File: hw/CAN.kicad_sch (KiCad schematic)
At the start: 16 parts, among them IC1 MCP2518FDT-E_SL, IC2 MCP2518FDT-E_SL, IC7 ADM3050EBRIZ, IC8 ADM3050EBRIZ, Y1 ABM8-20.000MHZ-10-B1U-T, Y2 ABM8-20.000MHZ-10-B1U-T

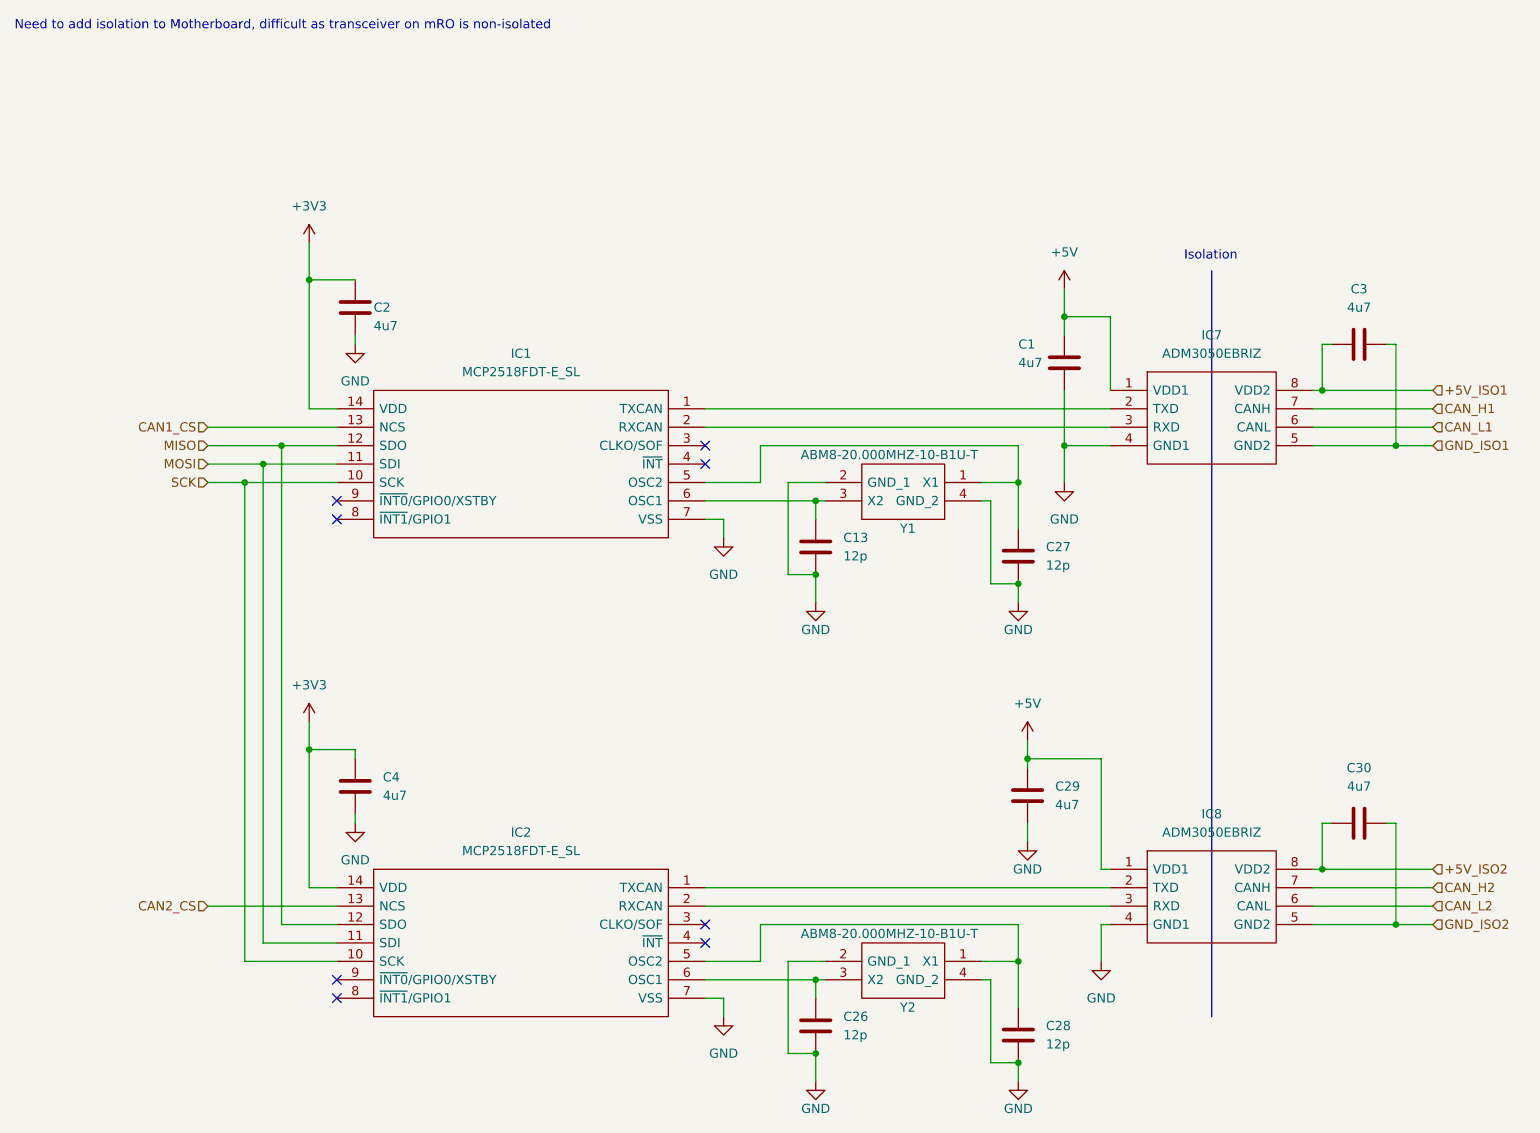
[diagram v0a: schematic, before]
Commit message: connected interrupt pins to CAN controller
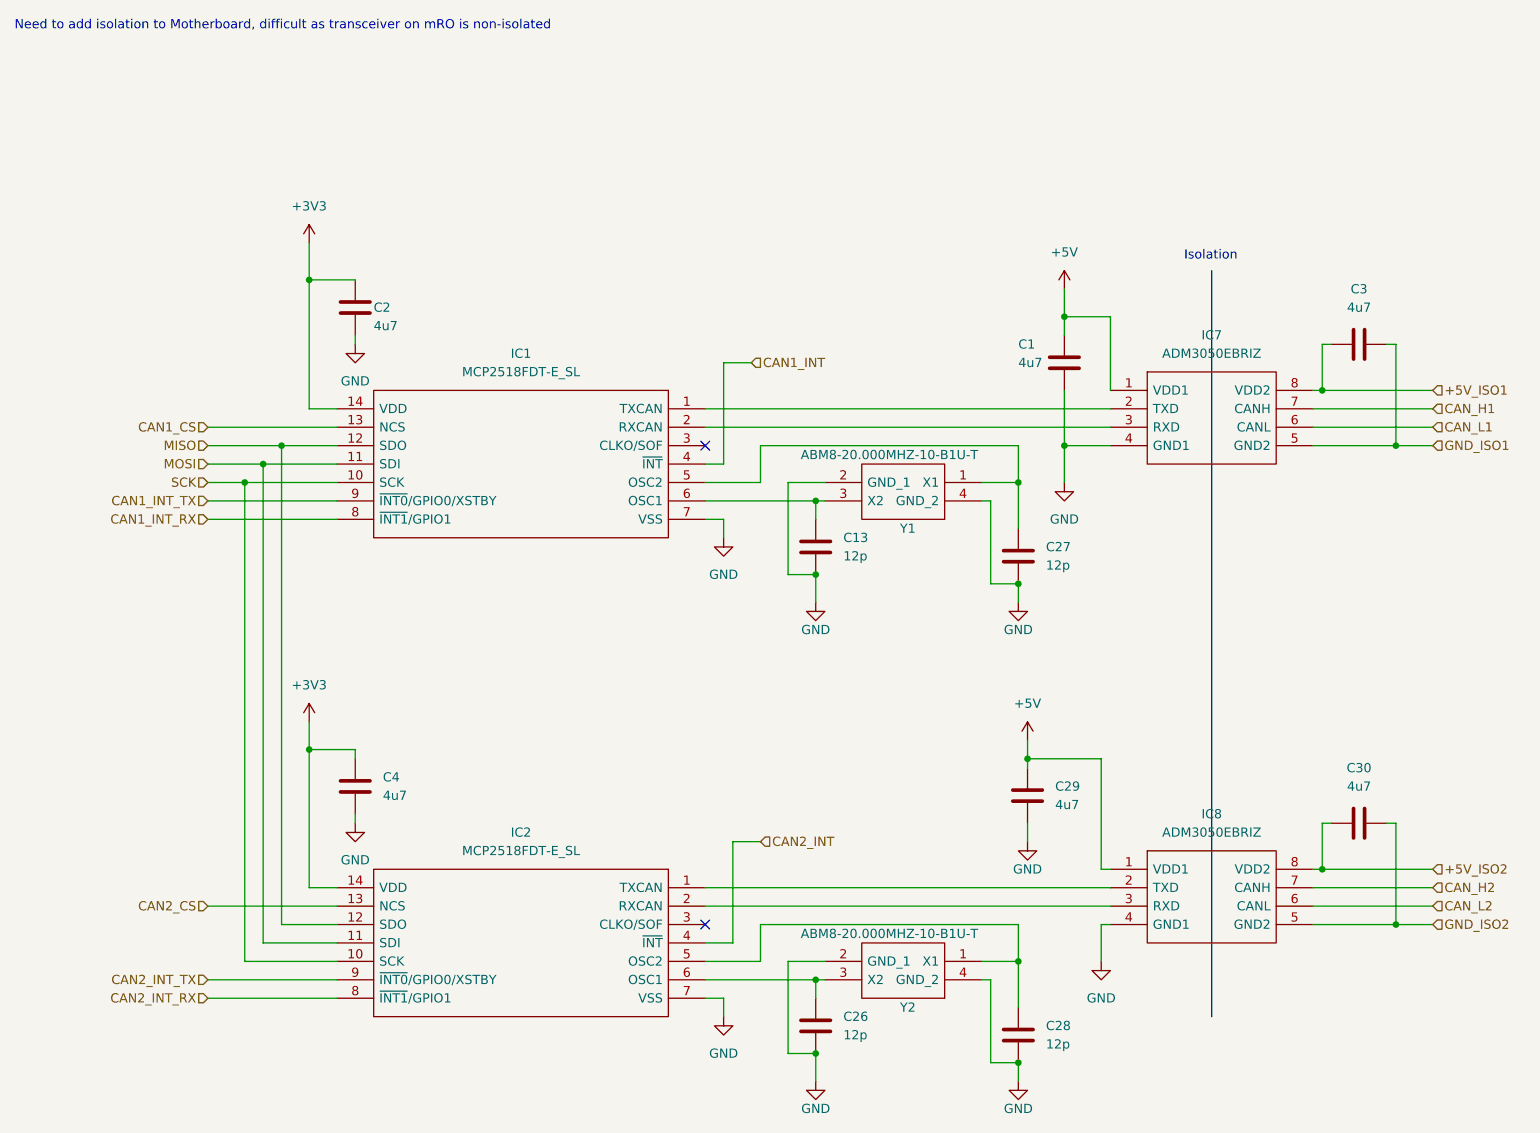
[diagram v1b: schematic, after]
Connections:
- net CAN1_INT: now reaches IC1.4 (~{INT})
- net CAN1_INT_RX: now reaches IC1.8 (~{INT1}/GPIO1)
- net CAN1_INT_TX: now reaches IC1.9 (~{INT0}/GPIO0/XSTBY)
- net CAN2_INT: now reaches IC2.4 (~{INT})
- net CAN2_INT_RX: now reaches IC2.8 (~{INT1}/GPIO1)
- net CAN2_INT_TX: now reaches IC2.9 (~{INT0}/GPIO0/XSTBY)
- no-connect marks 8 -> 2
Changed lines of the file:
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@@
   (junction (at 158.75 57.15) (diameter 0) (color 0 0 0 0)
   )
-  (no_connect (at 58.42 151.13))
-  (no_connect (at 58.42 85.09))
   (no_connect (at 109.22 74.93))
-  (no_connect (at 109.22 77.47))
-  (no_connect (at 58.42 82.55))
   (no_connect (at 109.22 140.97))
-  (no_connect (at 109.22 143.51))
-  (no_connect (at 58.42 148.59))
   (wire (pts (xy 120.65 158.75) (xy 124.46 158.75))
     (stroke (width 0) (type default) (color 0 0 0 0))
@@
     (stroke (width 0) (type default) (color 0 0 0 0))
   )
+  (wire (pts (xy 109.22 77.47) (xy 111.76 77.47))
+    (stroke (width 0) (type default) (color 0 0 0 0))
+  )
   (wire (pts (xy 148.59 82.55) (xy 148.59 93.98))
     (stroke (width 0) (type default) (color 0 0 0 0))
@@
     (stroke (width 0) (type default) (color 0 0 0 0))
   )
+  (wire (pts (xy 113.03 129.54) (xy 113.03 143.51))
+    (stroke (width 0) (type default) (color 0 0 0 0))
+  )
   (wire (pts (xy 58.42 143.51) (xy 48.26 143.51))
     (stroke (width 0) (type default) (color 0 0 0 0))
   )
+  (wire (pts (xy 111.76 63.5) (xy 115.57 63.5))
+    (stroke (width 0) (type default) (color 0 0 0 0))
+  )
   (wire (pts (xy 124.46 82.55) (xy 124.46 85.09))
     (stroke (width 0) (type default) (color 0 0 0 0))
@@
     (stroke (width 0) (type default) (color 0 0 0 0))
   )
+  (wire (pts (xy 111.76 77.47) (xy 111.76 63.5))
+    (stroke (width 0) (type default) (color 0 0 0 0))
+  )
   (wire (pts (xy 58.42 140.97) (xy 50.8 140.97))
     (stroke (width 0) (type default) (color 0 0 0 0))
@@
     (stroke (width 0) (type default) (color 0 0 0 0))
   )
+  (wire (pts (xy 116.84 129.54) (xy 113.03 129.54))
+    (stroke (width 0) (type default) (color 0 0 0 0))
+  )
   (wire (pts (xy 165.1 57.15) (xy 158.75 57.15))
     (stroke (width 0) (type default) (color 0 0 0 0))
@@
     (stroke (width 0) (type default) (color 0 0 0 0))
   )
+  (wire (pts (xy 40.64 151.13) (xy 58.42 151.13))
+    (stroke (width 0) (type default) (color 0 0 0 0))
+  )
   (wire (pts (xy 116.84 140.97) (xy 152.4 140.97))
     (stroke (width 0) (type default) (color 0 0 0 0))
@@
     (stroke (width 0) (type default) (color 0 0 0 0))
   )
+  (wire (pts (xy 40.64 148.59) (xy 58.42 148.59))
+    (stroke (width 0) (type default) (color 0 0 0 0))
+  )
   (wire (pts (xy 40.64 72.39) (xy 58.42 72.39))
     (stroke (width 0) (type default) (color 0 0 0 0))
@@
     (stroke (width 0) (type default) (color 0 0 0 0))
   )
+  (wire (pts (xy 40.64 85.09) (xy 58.42 85.09))
+    (stroke (width 0) (type default) (color 0 0 0 0))
+  )
   (wire (pts (xy 148.59 148.59) (xy 147.32 148.59))
     (stroke (width 0) (type default) (color 0 0 0 0))
@@
     (stroke (width 0) (type default) (color 0 0 0 0))
   )
+  (wire (pts (xy 113.03 143.51) (xy 109.22 143.51))
+    (stroke (width 0) (type default) (color 0 0 0 0))
+  )
   (wire (pts (xy 194.31 127) (xy 195.58 127))
     (stroke (width 0) (type default) (color 0 0 0 0))
@@
   )
   (wire (pts (xy 153.67 115.57) (xy 153.67 118.11))
+    (stroke (width 0) (type default) (color 0 0 0 0))
+  )
+  (wire (pts (xy 40.64 82.55) (xy 58.42 82.55))
     (stroke (width 0) (type default) (color 0 0 0 0))
   )
@@
     (effects (font (size 1.27 1.27)) (justify left bottom))
   )
+  (hierarchical_label "CAN2_INT" (shape input) (at 116.84 129.54 0)
+    (effects (font (size 1.27 1.27)) (justify left))
+  )
   (hierarchical_label "CAN2_CS" (shape input) (at 40.64 138.43 180)
     (effects (font (size 1.27 1.27)) (justify right))
@@
     (effects (font (size 1.27 1.27)) (justify left))
   )
+  (hierarchical_label "CAN1_INT" (shape input) (at 115.57 63.5 0)
+    (effects (font (size 1.27 1.27)) (justify left))
+  )
   (hierarchical_label "CAN_L2" (shape input) (at 209.55 138.43 0)
     (effects (font (size 1.27 1.27)) (justify left))
@@
     (effects (font (size 1.27 1.27)) (justify right))
   )
+  (hierarchical_label "CAN2_INT_TX" (shape input) (at 40.64 148.59 180)
+    (effects (font (size 1.27 1.27)) (justify right))
+  )
+  (hierarchical_label "CAN1_INT_TX" (shape input) (at 40.64 82.55 180)
+    (effects (font (size 1.27 1.27)) (justify right))
+  )
   (hierarchical_label "+5V_ISO1" (shape input) (at 209.55 67.31 0)
     (effects (font (size 1.27 1.27)) (justify left))
   )
+  (hierarchical_label "CAN2_INT_RX" (shape input) (at 40.64 151.13 180)
+    (effects (font (size 1.27 1.27)) (justify right))
+  )
+  (hierarchical_label "CAN1_INT_RX" (shape input) (at 40.64 85.09 180)
+    (effects (font (size 1.27 1.27)) (justify right))
+  )
   (hierarchical_label "SCK" (shape input) (at 40.64 80.01 180)

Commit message: update comments
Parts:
- C1, C2, C29, C3, C30, C4: Manufacturer_Name (none) -> Murata; Manufacturer_Part_Number (none) -> GRT188C81E475KE13D
- C13, C26, C27, C28: Manufacturer_Name (none) -> Murata; Manufacturer_Part_Number (none) -> GCM1885C1H120GA16D
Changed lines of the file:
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@@
+      (effects (font (size 1.27 1.27)) hide)
+    )
+    (property "Manufacturer_Name" "Murata" (id 4) (at 199.39 127 0)
+      (effects (font (size 1.27 1.27)) hide)
+    )
+    (property "Manufacturer_Part_Number" "GRT188C81E475KE13D " (id 5) (at 199.39 127 0)
       (effects (font (size 1.27 1.27)) hide)
     )
@@
       (effects (font (size 1.27 1.27)) hide)
     )
+    (property "Manufacturer_Name" "Murata" (id 4) (at 152.4 90.17 0)
+      (effects (font (size 1.27 1.27)) hide)
+    )
+    (property "Manufacturer_Part_Number" "GCM1885C1H120GA16D " (id 5) (at 152.4 90.17 0)
+      (effects (font (size 1.27 1.27)) hide)
+    )
     (pin "1")
     (pin "2")
@@
       (effects (font (size 1.27 1.27)) hide)
     )
+    (property "Manufacturer_Name" "Murata" (id 4) (at 158.75 63.5 0)
+      (effects (font (size 1.27 1.27)) hide)
+    )
+    (property "Manufacturer_Part_Number" "GRT188C81E475KE13D " (id 5) (at 158.75 63.5 0)
+      (effects (font (size 1.27 1.27)) hide)
+    )
     (pin "1")
     (pin "2")
@@
     )
     (property "Datasheet" "~" (id 3) (at 152.4 156.21 0)
+      (effects (font (size 1.27 1.27)) hide)
+    )
+    (property "Manufacturer_Name" "Murata" (id 4) (at 152.4 156.21 0)
+      (effects (font (size 1.27 1.27)) hide)
+    )
+    (property "Manufacturer_Part_Number" "GCM1885C1H120GA16D " (id 5) (at 152.4 156.21 0)
       (effects (font (size 1.27 1.27)) hide)
     )
@@
       (effects (font (size 1.27 1.27)) hide)
     )
+    (property "Manufacturer_Name" "Murata" (id 4) (at 60.96 121.92 0)
+      (effects (font (size 1.27 1.27)) hide)
+    )
+    (property "Manufacturer_Part_Number" "GRT188C81E475KE13D " (id 5) (at 60.96 121.92 0)
+      (effects (font (size 1.27 1.27)) hide)
+    )
     (pin "1")
     (pin "2")
@@
     )
     (property "Datasheet" "~" (id 3) (at 124.46 88.9 0)
+      (effects (font (size 1.27 1.27)) hide)
+    )
+    (property "Manufacturer_Name" "Murata" (id 4) (at 124.46 88.9 0)
+      (effects (font (size 1.27 1.27)) hide)
+    )
+    (property "Manufacturer_Part_Number" "GCM1885C1H120GA16D " (id 5) (at 124.46 88.9 0)
       (effects (font (size 1.27 1.27)) hide)
     )
@@
       (effects (font (size 1.27 1.27)) hide)
     )
+    (property "Manufacturer_Name" "Murata" (id 4) (at 199.39 60.96 0)
+      (effects (font (size 1.27 1.27)) hide)
+    )
+    (property "Manufacturer_Part_Number" "GRT188C81E475KE13D " (id 5) (at 199.39 60.96 0)
+      (effects (font (size 1.27 1.27)) hide)
+    )
     (pin "1")
     (pin "2")
@@
       (effects (font (size 1.27 1.27)) hide)
     )
+    (property "Manufacturer_Name" "Murata" (id 4) (at 124.46 154.94 0)
+      (effects (font (size 1.27 1.27)) hide)
+    )
+    (property "Manufacturer_Part_Number" "GCM1885C1H120GA16D " (id 5) (at 124.46 154.94 0)
+      (effects (font (size 1.27 1.27)) hide)
+    )
     (pin "1")
     (pin "2")
@@
       (effects (font (size 1.27 1.27)) hide)
     )
+    (property "Manufacturer_Name" "Murata" (id 4) (at 60.96 55.88 0)
+      (effects (font (size 1.27 1.27)) hide)
+    )
+    (property "Manufacturer_Part_Number" "GRT188C81E475KE13D " (id 5) (at 60.96 55.88 0)
+      (effects (font (size 1.27 1.27)) hide)
+    )
     (pin "1")
     (pin "2")
@@
       (effects (font (size 1.27 1.27)) hide)
     )
+    (property "Manufacturer_Name" "Murata" (id 4) (at 153.67 123.19 0)
+      (effects (font (size 1.27 1.27)) hide)
+    )
+    (property "Manufacturer_Part_Number" "GRT188C81E475KE13D " (id 5) (at 153.67 123.19 0)
+      (effects (font (size 1.27 1.27)) hide)
+    )
